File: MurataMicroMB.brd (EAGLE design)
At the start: 90 x 63 mm, 52 parts, among them CON1 C-2395, CON2 WM17143CT-ND, CON3 CON_MIL_10_ARM, CON4 C-2395, IC1 NC7SZ00M5XCT-ND, IC2 296-35164-1-ND, IC3 IC_LPC11U3XQFN33, IC4 AZ1117EH-3.3TRG1DICT-ND, Q1 1253-1168-1-ND, SW1 P-8073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

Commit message: [ FIX ] library update
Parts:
- removed TP1, TP2: TPPAD1-13, testpad_local:P1-13
- added TP3, TP4, TP5: TESTPAD_F, mylib:FIDUCIAL
- added X2: TSW-102-02-S-S, con-samtec.local:TSW-102-02-S-S
- R15, R16, R5, R6: value 100/1005 -> 33/1005
- moved SW1 4.10 mm to (65.0, 45.1)
- moved SW2 2.90 mm to (60.0, 45.1)
- moved SW3 1.70 mm to (55.0, 45.1)
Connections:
- net GND: now also X2.2; no longer TP2.TP
- net VPP: now also X2.1; no longer TP1.TP
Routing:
- net !RESET!: track 27.9 -> 32.0 mm
- net BL: track 22.1 -> 25.0 mm
- net ISP: track 20.4 -> 22.1 mm
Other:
- outline, holes or cut-outs redrawn
- board text added: "r0.2"
- board text removed: "r0.1"

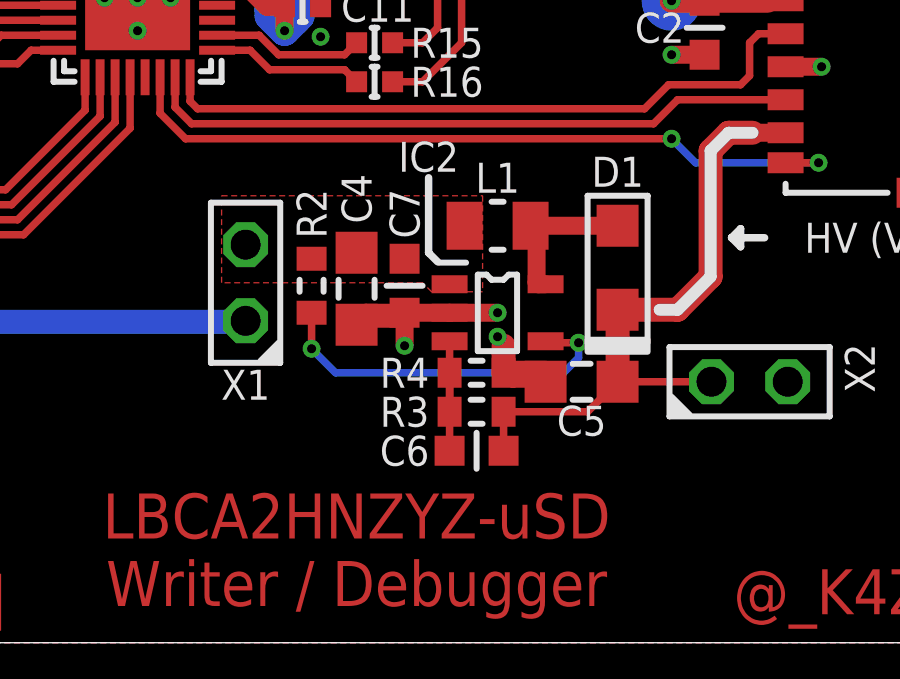
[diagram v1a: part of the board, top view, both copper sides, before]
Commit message: [ MB ] resize R2 and C7
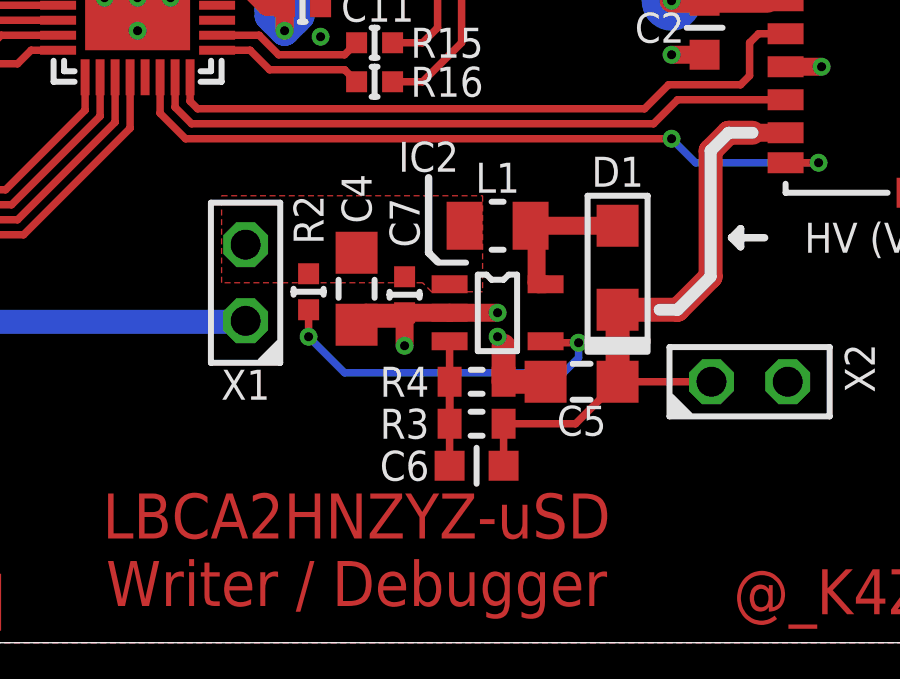
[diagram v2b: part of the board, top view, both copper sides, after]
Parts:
- C7: value 0.1u/1608 -> 0.1u/1005; device mylib:CR_1608 -> mylib:C0402
- R2: value 10k/1608 -> 10k/1005; device mylib:R_1608_PADPAD -> mylib:C0402
- moved C6 0.50 mm to (53.3, 15.9)
- moved R3 0.40 mm to (53.3, 17.3)
- moved R4 0.30 mm to (53.3, 18.7)
- moved C7 0.30 mm to (50.9, 21.6)
- moved R2 0.22 mm to (47.7, 21.7)
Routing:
- net GND: track 21.0 -> 19.8 mm
- net N$10: track 4.95 -> 5.55 mm
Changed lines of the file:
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@@
 <wire x1="61.7" y1="26.1" x2="62" y2="26.4" width="0.25" layer="41"/>
 <wire x1="62" y1="26.4" x2="62.3" y2="26.4" width="0.25" layer="41"/>
-<wire x1="53.7" y1="15.7" x2="55" y2="15.7" width="0.25" layer="41"/>
-<wire x1="55" y1="15.7" x2="55" y2="17.3" width="0.25" layer="41"/>
+<wire x1="53.7" y1="15.2" x2="55" y2="15.2" width="0.25" layer="41"/>
+<wire x1="55" y1="15.2" x2="55" y2="17.3" width="0.25" layer="41"/>
 <wire x1="55" y1="17.3" x2="62.4" y2="17.3" width="0.25" layer="41"/>
 <wire x1="59" y1="20.5" x2="59" y2="19.2" width="0.25" layer="41"/>
@@
 <attribute name="NAME" x="58" y="25.7" size="1" layer="25" font="vector" ratio="20" rot="R180" align="center"/>
 </element>
-<element name="R2" library="mylib" package="R_1608_PADPAD" value="10k/1608" x="47.8" y="21.9" smashed="yes" rot="R90">
-<attribute name="NAME" x="47.8" y="24.3" size="1" layer="25" font="vector" ratio="20" rot="R270" align="center"/>
-<attribute name="VALUE" x="50" y="21.3" size="1.27" layer="27" font="vector" ratio="15" rot="R90"/>
-</element>
-<element name="R3" library="mylib" package="R_1608_PADPAD" value="P60.4KHCT-ND" x="53.3" y="17.7" smashed="yes">
-<attribute name="NAME" x="50.9" y="17.7" size="1" layer="25" font="vector" ratio="20" align="center"/>
-<attribute name="VALUE" x="52.665" y="15.4775" size="1.27" layer="27" font="vector" ratio="15"/>
-</element>
-<element name="R4" library="mylib" package="R_1608_PADPAD" value="P13.3KHCT-ND" x="53.3" y="19" smashed="yes" rot="R180">
-<attribute name="NAME" x="50.9" y="19" size="1" layer="25" font="vector" ratio="20" align="center"/>
-<attribute name="VALUE" x="53.935" y="21.2225" size="1.27" layer="27" font="vector" ratio="15" rot="R180"/>
+<element name="R2" library="mylib" package="C0402" value="10k/1005" x="47.7" y="21.7" smashed="yes" rot="R90">
+<attribute name="NAME" x="47.7" y="24.1" size="1" layer="25" font="vector" ratio="20" rot="R270" align="center"/>
+<attribute name="VALUE" x="49.9" y="21.1" size="1.27" layer="27" font="vector" ratio="15" rot="R90"/>
+</element>
+<element name="R3" library="mylib" package="R_1608_PADPAD" value="P60.4KHCT-ND" x="53.3" y="17.3" smashed="yes">
+<attribute name="NAME" x="50.9" y="17.3" size="1" layer="25" font="vector" ratio="20" align="center"/>
+<attribute name="VALUE" x="52.665" y="15.0775" size="1.27" layer="27" font="vector" ratio="15"/>
+</element>
+<element name="R4" library="mylib" package="R_1608_PADPAD" value="P13.3KHCT-ND" x="53.3" y="18.7" smashed="yes" rot="R180">
+<attribute name="NAME" x="50.9" y="18.7" size="1" layer="25" font="vector" ratio="20" align="center"/>
+<attribute name="VALUE" x="53.935" y="20.9225" size="1.27" layer="27" font="vector" ratio="15" rot="R180"/>
 </element>
 <element name="C4" library="mylib" package="CR_2125" value="4.7u/2012" x="49.3" y="21.8" smashed="yes" rot="R270">
@@
 <attribute name="VALUE" x="56.9" y="20.2" size="1.27" layer="27" font="vector" ratio="15" rot="R180" align="center"/>
 </element>
-<element name="C6" library="mylib" package="CR_1608" value="NM/1608" x="53.3" y="16.4" smashed="yes" rot="R180">
-<attribute name="NAME" x="50.9" y="16.4" size="1" layer="25" font="vector" ratio="20" rot="R180" align="center"/>
-<attribute name="VALUE" x="53.4" y="17.9" size="1.27" layer="27" font="vector" ratio="15" rot="R180" align="center"/>
+<element name="C6" library="mylib" package="CR_1608" value="NM/1608" x="53.3" y="15.9" smashed="yes" rot="R180">
+<attribute name="NAME" x="50.9" y="15.9" size="1" layer="25" font="vector" ratio="20" rot="R180" align="center"/>
+<attribute name="VALUE" x="53.4" y="17.4" size="1.27" layer="27" font="vector" ratio="15" rot="R180" align="center"/>
 </element>
 <element name="X1" library="con-samtec.local" package="TSW-102-02-S-S" value="TSW-102-02-S-S" x="45.6" y="22" smashed="yes" rot="R270">
@@
 <attribute name="VALUE" x="44.33" y="17.555" size="1" layer="27" font="vector" ratio="20"/>
 </element>
-<element name="C7" library="mylib" package="CR_1608" value="0.1u/1608" x="50.9" y="21.9" smashed="yes" rot="R270">
-<attribute name="NAME" x="50.9" y="24.3" size="1" layer="25" font="vector" ratio="20" rot="R90" align="center"/>
-<attribute name="VALUE" x="49.4" y="22" size="1.27" layer="27" font="vector" ratio="15" rot="R270" align="center"/>
+<element name="C7" library="mylib" package="C0402" value="0.1u/1005" x="50.9" y="21.6" smashed="yes" rot="R270">
+<attribute name="NAME" x="50.9" y="24" size="1" layer="25" font="vector" ratio="20" rot="R90" align="center"/>
+<attribute name="VALUE" x="49.4" y="21.7" size="1.27" layer="27" font="vector" ratio="15" rot="R270" align="center"/>
 </element>
 <element name="IC3" library="mylib" package="HVQFN33" value="IC_LPC11U3XQFN33" x="42" y="31.5" smashed="yes" rot="R270">
@@
 <via x="54" y="21" extent="1-16" drill="0.3"/>
 <via x="54" y="20.2" extent="1-16" drill="0.3"/>
-<wire x1="54.2" y1="19" x2="54.5" y2="18.7" width="0.4" layer="1"/>
-<wire x1="54.5" y1="18.7" x2="55.6" y2="18.7" width="0.4" layer="1"/>
-<wire x1="54.2" y1="19" x2="55.6" y2="19" width="0.8" layer="1"/>
-<wire x1="54.2" y1="19" x2="54.2" y2="19.9" width="0.8" layer="1"/>
+<wire x1="54.2" y1="18.7" x2="54.2" y2="19.9" width="0.8" layer="1"/>
 <contactref element="C7" pad="2"/>
 <wire x1="49.6" y1="20.9" x2="50.9" y2="20.9" width="0.8" layer="1"/>
@@
 <contactref element="LED1" pad="3"/>
 <contactref element="X2" pad="2"/>
+<wire x1="54.2" y1="18.7" x2="55.6" y2="18.7" width="0.8" layer="1"/>
 </signal>
 <signal name="D-">
@@
 <contactref element="C5" pad="1"/>
 <contactref element="R3" pad="2"/>
-<wire x1="54.2" y1="17.7" x2="57" y2="17.7" width="0.25" layer="1"/>
-<wire x1="57" y1="17.7" x2="58" y2="18.7" width="0.25" layer="1"/>
-<wire x1="54.2" y1="17.7" x2="54.2" y2="16.4" width="0.25" layer="1"/>
+<wire x1="54.2" y1="17.3" x2="56.6" y2="17.3" width="0.25" layer="1"/>
+<wire x1="56.6" y1="17.3" x2="58" y2="18.7" width="0.25" layer="1"/>
+<wire x1="54.2" y1="17.3" x2="54.2" y2="15.9" width="0.25" layer="1"/>
 <wire x1="63.6" y1="27" x2="62.5" y2="27" width="0.6" layer="1"/>
 <wire x1="62.5" y1="27" x2="61.7" y2="27" width="0.8" layer="1"/>
@@
 <wire x1="56.7" y1="20" x2="56.7" y2="19.5" width="0.25" layer="16"/>
 <wire x1="56.7" y1="19.5" x2="56.2" y2="19" width="0.25" layer="16"/>
-<wire x1="56.2" y1="19" x2="48.6" y2="19" width="0.25" layer="16"/>
-<wire x1="48.6" y1="19" x2="47.8" y2="19.8" width="0.25" layer="16"/>
-<via x="47.8" y="19.8" extent="1-16" drill="0.3"/>
-<wire x1="47.8" y1="19.8" x2="47.8" y2="21" width="0.25" layer="1"/>
+<wire x1="56.2" y1="19" x2="48.9" y2="19" width="0.25" layer="16"/>
+<wire x1="48.9" y1="19" x2="47.7" y2="20.2" width="0.25" layer="16"/>
+<via x="47.7" y="20.2" extent="1-16" drill="0.3"/>
+<wire x1="47.7" y1="20.2" x2="47.7" y2="21.1" width="0.25" layer="1"/>
 </signal>
 <signal name="N$10">
@@
 <contactref element="R4" pad="2"/>
 <contactref element="C6" pad="2"/>
-<wire x1="52.4" y1="17.7" x2="52.4" y2="16.4" width="0.25" layer="1"/>
-<wire x1="52.4" y1="19" x2="52.4" y2="17.7" width="0.25" layer="1"/>
-<wire x1="52.4" y1="17.7" x2="52.4" y2="20.05" width="0.25" layer="1"/>
+<wire x1="52.4" y1="17.3" x2="52.4" y2="15.9" width="0.25" layer="1"/>
+<wire x1="52.4" y1="18.7" x2="52.4" y2="17.3" width="0.25" layer="1"/>
+<wire x1="52.4" y1="17.3" x2="52.4" y2="20.05" width="0.25" layer="1"/>
 </signal>
 <signal name="N$6">

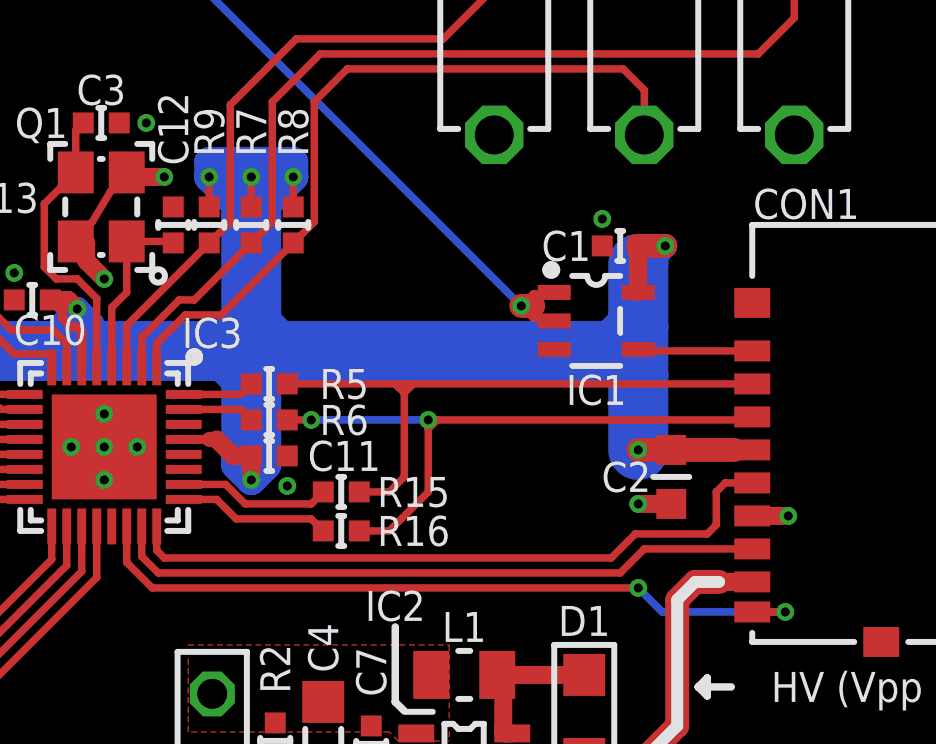
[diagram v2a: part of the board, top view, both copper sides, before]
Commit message: [ MB ] R5/6/15/16 moved; add DETECT1/2 pin on schematic
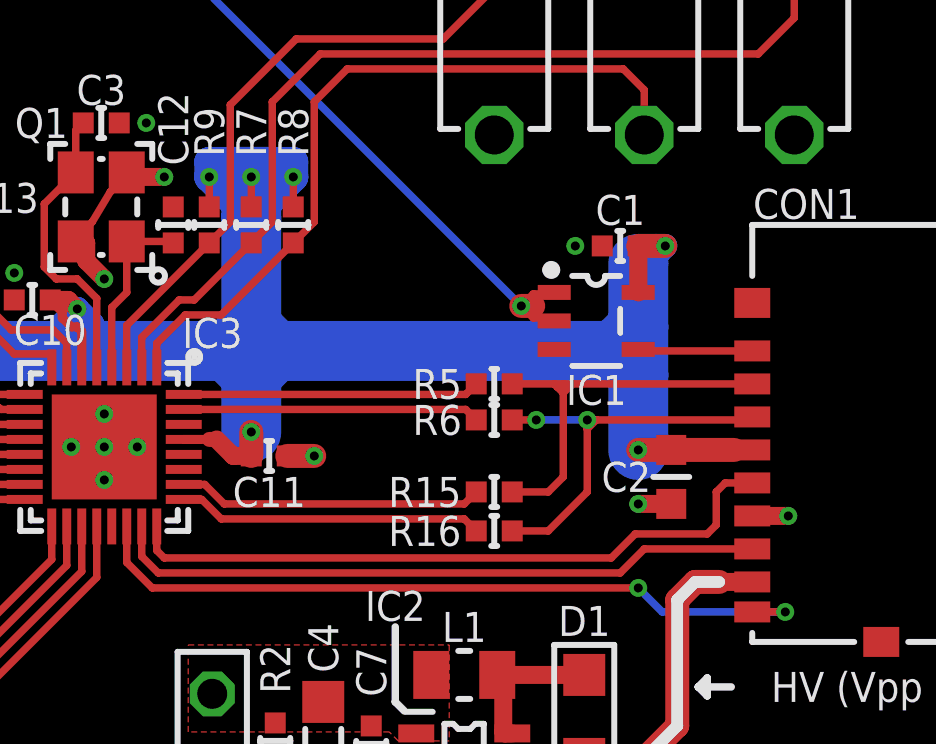
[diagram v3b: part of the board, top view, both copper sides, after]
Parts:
- moved R5 7.50 mm to (55.0, 33.6)
- moved R6 7.50 mm to (55.0, 32.4)
- moved R15 5.10 mm to (55.0, 30.0)
- moved R16 5.10 mm to (55.0, 28.7)
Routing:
- net N$9: track 2.39 -> 9.89 mm
- net N$6: track 2.39 -> 9.89 mm
- net MOSI: track 21.2 -> 13.9 mm
- net !CS!: track 21.6 -> 14.3 mm
- net N$18: track 5.08 -> 10.2 mm
- net N$17: track 5.08 -> 10.2 mm
- net 3.3V: track 135.6 -> 131.2 mm
- net GND: track 19.8 -> 20.7 mm
